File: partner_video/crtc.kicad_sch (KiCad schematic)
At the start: 37 parts, among them J3 Monitor, J4 Brightness pot, T4 BC109, U1 74LS166, U10 74LS123, U13 74LS74, U16 74LS123, U18 74LS163, U2 8275, U21 74LS86, U26 74S04, U3 74LS175, U4 2732, U5 74LS175, U7 74LS10, Y2 22.780 Mhz

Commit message: Update custom symbol attributes
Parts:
- U4: footprint Package_DIP:DIP-24_W15.24mm -> (none)
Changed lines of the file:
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@@
       (effects (font (size 1.27 1.27)) (justify left))
     )
-    (property "Footprint" "Package_DIP:DIP-24_W15.24mm" (at 209.55 60.96 0)
-      (effects (font (size 1.27 1.27)) hide)
-    )
-    (property "Datasheet" "" (at 185.42 57.15 0)
+    (property "Footprint" "" (at 209.55 60.96 0)
+      (effects (font (size 1.27 1.27)) hide)
+    )
+    (property "Datasheet" "http://ee.hawaii.edu/~sasaki/EE260/Labs/Datasheets/m2732a.pdf" (at 185.42 57.15 0)
       (effects (font (size 1.27 1.27)) hide)
     )
@@
       (effects (font (size 1.27 1.27)) hide)
     )
-    (property "Datasheet" "" (at 77.47 54.61 0)
-      (effects (font (size 1.27 1.27)) hide)
-    )
+    (property "Datasheet" "https://www.jameco.com/Jameco/Products/ProdDS/52821.pdf" (at 77.47 54.61 0)
+      (effects (font (size 1.27 1.27)) hide)
+    )

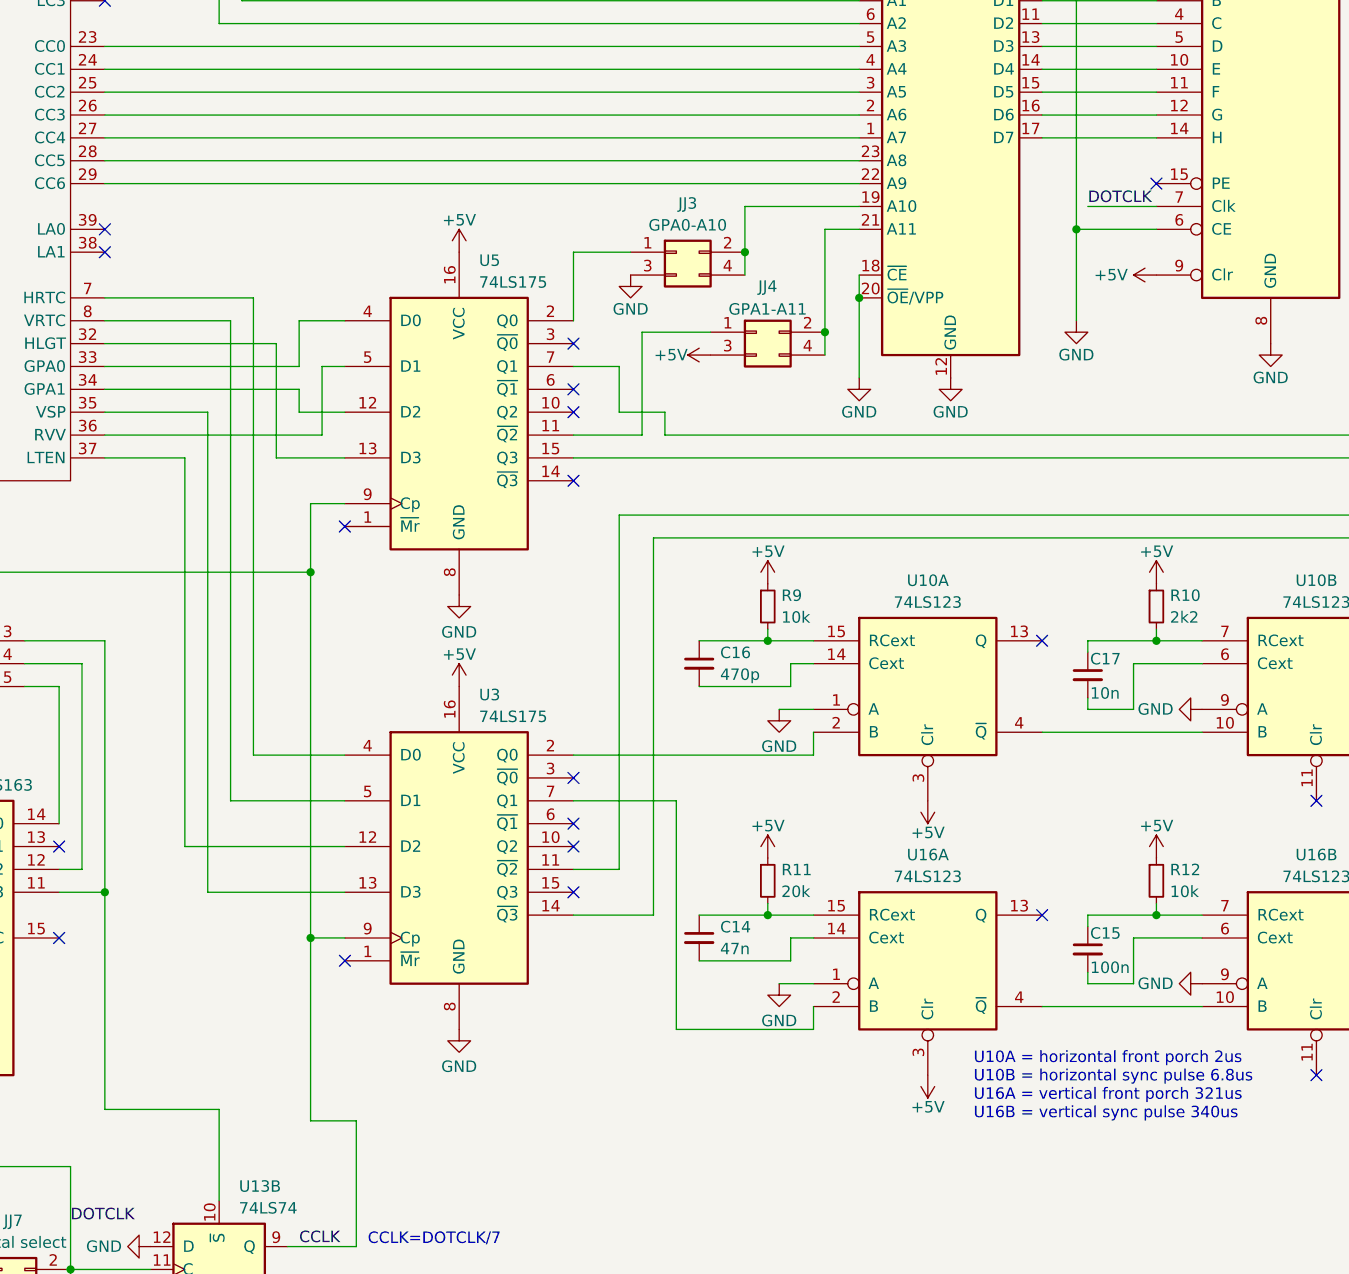
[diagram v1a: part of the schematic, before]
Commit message: Add missing ~{CLOAD} signal to U1
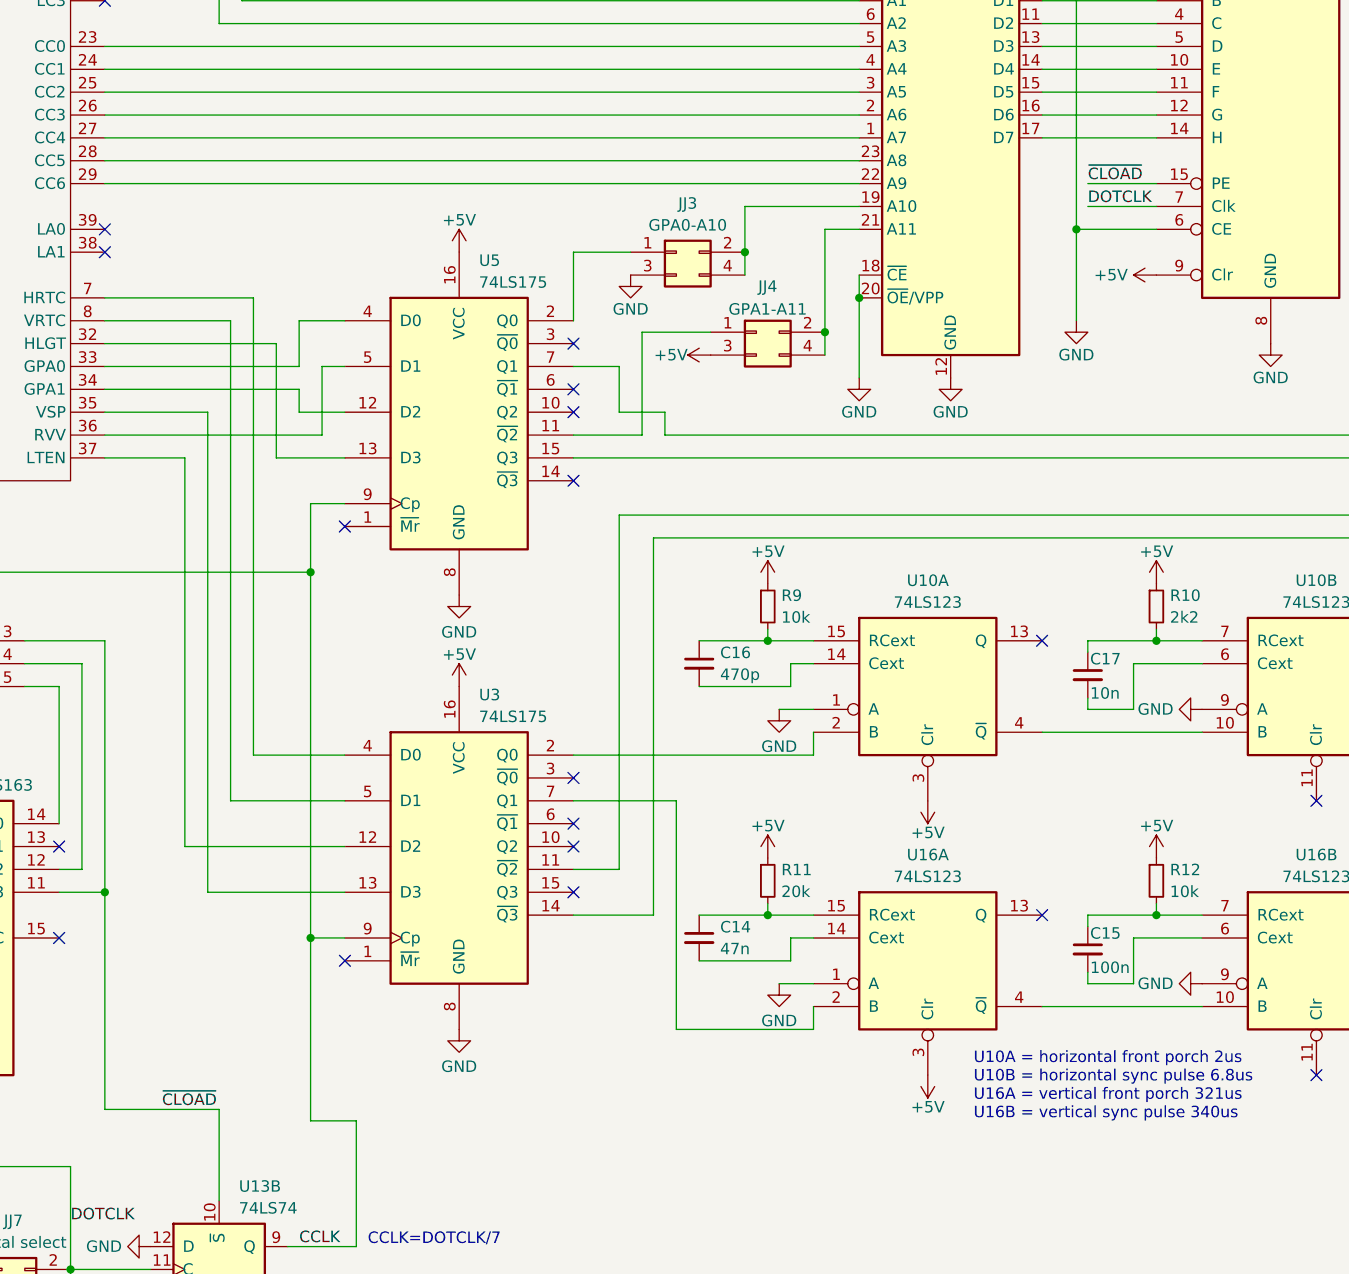
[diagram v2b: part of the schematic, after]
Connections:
- net ~{CLOAD}: now reaches U1.15 (PE)
- net ~{CLOAD}: now also U13.10 (~{S}), U18.11 (Q3), U7.3
- no-connect marks 27 -> 26
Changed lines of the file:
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@@
   (no_connect (at 143.51 85.09))
   (no_connect (at 111.76 182.88))
-  (no_connect (at 208.28 59.69))
   (no_connect (at 63.5 172.72))
   (no_connect (at 143.51 92.71))
@@
     (stroke (width 0) (type default))
   )
+  (wire (pts (xy 200.66 59.69) (xy 208.28 59.69))
+    (stroke (width 0) (type default))
+  )
   (wire (pts (xy 143.51 135.89) (xy 148.59 135.89))
     (stroke (width 0) (type default))
@@
     (effects (font (size 1.27 1.27)) (justify left bottom))
   )
+  (label "~{CLOAD}" (at 200.66 59.69 0) (fields_autoplaced)
+    (effects (font (size 1.27 1.27)) (justify left bottom))
+  )
   (label "~{LTEN_B}" (at 252.73 44.45 0) (fields_autoplaced)
     (effects (font (size 1.27 1.27)) (justify left bottom))
@@
     (effects (font (size 1.27 1.27)) (justify left bottom))
   )
+  (label "~{CLOAD}" (at 97.79 162.56 0) (fields_autoplaced)
+    (effects (font (size 1.27 1.27)) (justify left bottom))
+  )

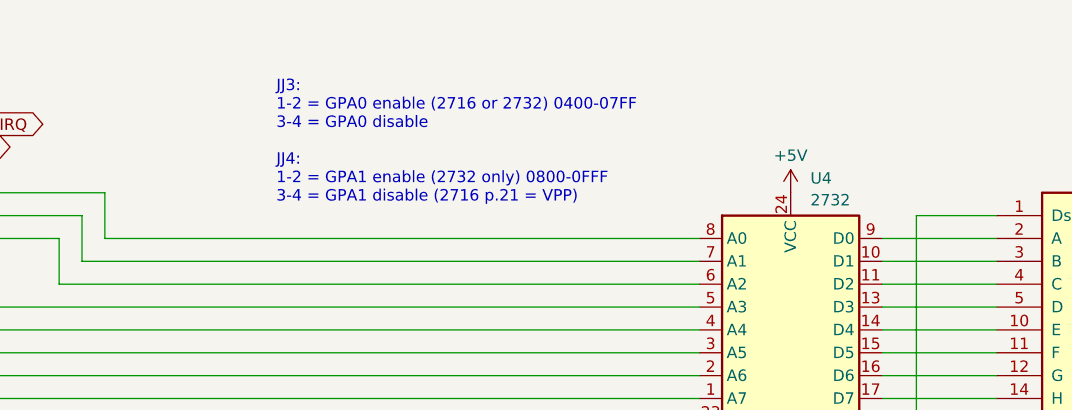
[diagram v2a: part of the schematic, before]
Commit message: Add note that GPA1 is inverted
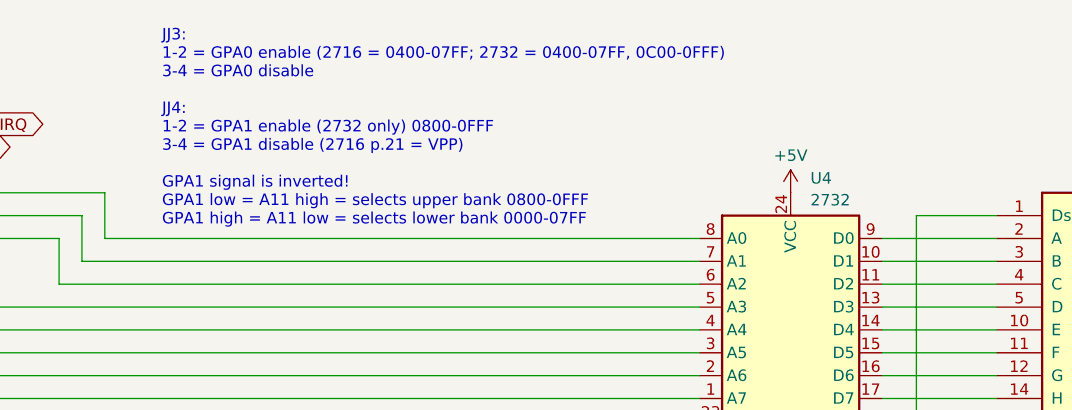
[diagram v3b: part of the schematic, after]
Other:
- note added: "JJ3: 1-2 = GPA0 enable (2716 = 0400-07FF; 2732 = 0400-07FF, 0C00-0FFF) 3-4 = GPA0 disable JJ4: 1-2 = GPA1 enable (2732 only) 0800-0FFF 3-4 = GPA1 disable (2716 p.21 = VPP) GPA1 signal is inverted! GPA1 low = A11 high = selects upper bank 0800-0FFF GPA1 high = A11 low = selects lower bank 0000-07FF"
- note removed: "JJ3: 1-2 = GPA0 enable (2716 or 2732) 0400-07FF 3-4 = GPA0 disable JJ4: 1-2 = GPA1 enable (2732 only) 0800-0FFF 3-4 = GPA1 disable (2716 p.21 = VPP)"
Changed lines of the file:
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@@
     (effects (font (size 1.27 1.27)) (justify left bottom))
   )
-  (text "JJ3:\n1-2 = GPA0 enable (2716 or 2732) 0400-07FF\n3-4 = GPA0 disable\n\nJJ4:\n1-2 = GPA1 enable (2732 only) 0800-0FFF\n3-4 = GPA1 disable (2716 p.21 = VPP)"
-    (at 128.27 33.02 0)
+  (text "JJ3:\n1-2 = GPA0 enable (2716 = 0400-07FF; 2732 = 0400-07FF, 0C00-0FFF)\n3-4 = GPA0 disable\n\nJJ4:\n1-2 = GPA1 enable (2732 only) 0800-0FFF\n3-4 = GPA1 disable (2716 p.21 = VPP)\n\nGPA1 signal is inverted!\nGPA1 low = A11 high = selects upper bank 0800-0FFF\nGPA1 high = A11 low = selects lower bank 0000-07FF"
+    (at 115.57 35.56 0)
     (effects (font (size 1.27 1.27)) (justify left bottom))
   )
